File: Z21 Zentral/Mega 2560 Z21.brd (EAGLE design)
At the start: 122 x 122.3 mm, 144 parts, among them IC1 TLE5205-2G, IC2 74AC244DW, IC3 LM358D, IC5 FT232RL, IC6 LTC485S, J1 RJ11, J2 RJ11, J3 RJ11, J5 RJ45-6L-B, J6 USB_MINI-B_SMT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

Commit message: Add files via upload
Changed 6 way power connector to allow connector to fit
Added PFET on input instead of Diode
Tidied up PCB Legends
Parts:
- removed D1: P600, diode:P6-15
- added D5: (no value), diode:SOT23
- added Q9: FDD4141TO252, transistor-fet:TO252
- added R31: 100k, rcl:R0603
- X9: device con-wago-508:W237-6P -> con-wago-500:W237-136
- moved B1 2.75 mm to (34.0, 97.0)
- moved K1 2.25 mm to (46.5, 97.5)
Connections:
- new net N$22: D5.1, Q9.1, R31.1
- net +18V: now also D5.3, Q9.2; no longer D1.C
- net GND: now also R31.2
- net N$23: now also Q9.3; no longer D1.A
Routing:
- net +18V: track 154.7 -> 187.4 mm
- net +12V: track 146.6 -> 151.4 mm
- net N$22: track 0.00 -> 3.62 mm
- net N$23: track 7.96 -> 11.3 mm
- net VCCIO: track 158.1 -> 154.9 mm
- net N$32: track 22.6 -> 24.7 mm
- net N$34: track 30.1 -> 32.1 mm
- net N$39: track 11.3 -> 9.79 mm
- net SSHORT: track 72.0 -> 73.2 mm
- net N$25: track 68.1 -> 67.0 mm
- net S2: track 62.0 -> 62.9 mm
- net XPB: track 65.5 -> 65.0 mm
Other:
- board text added: "Arduino Z21 DCC Zentrale IoT Tech & Philipp Gahtow July 2019"
- board text added: "S88"
- board text removed: "Arduino Z21 DCC Zentrale IoT Tech & Philipp Gahtow October 2018"

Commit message: Add files via upload
Added P Channel FET, replacing Diode
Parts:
- added IC4: (no value), v-reg:78XXS
- moved LED6 21.2 mm to (20.0, 78.0), turned to 90 degrees
- moved R51 17.9 mm to (20.0, 82.0)
- moved C11 0.90 mm to (18.2, 94.0)
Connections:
- net +12V: now also IC4.OUT
- net +18V: now also IC4.IN
- net GND: now also IC4.GND
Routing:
- net +18V: track 187.4 -> 172.8 mm
- net +12V: track 151.4 -> 153.6 mm
- net N$34: track 32.1 -> 30.2 mm
- net XNET_S/R: track 53.0 -> 51.1 mm
- net LN_OUT: track 78.7 -> 77.2 mm
- net XNET_TX: track 33.3 -> 32.0 mm
- net N$32: track 24.7 -> 23.3 mm
- net LN_IN: track 74.9 -> 73.9 mm
- net LN_RECEIVE: track 58.2 -> 57.3 mm

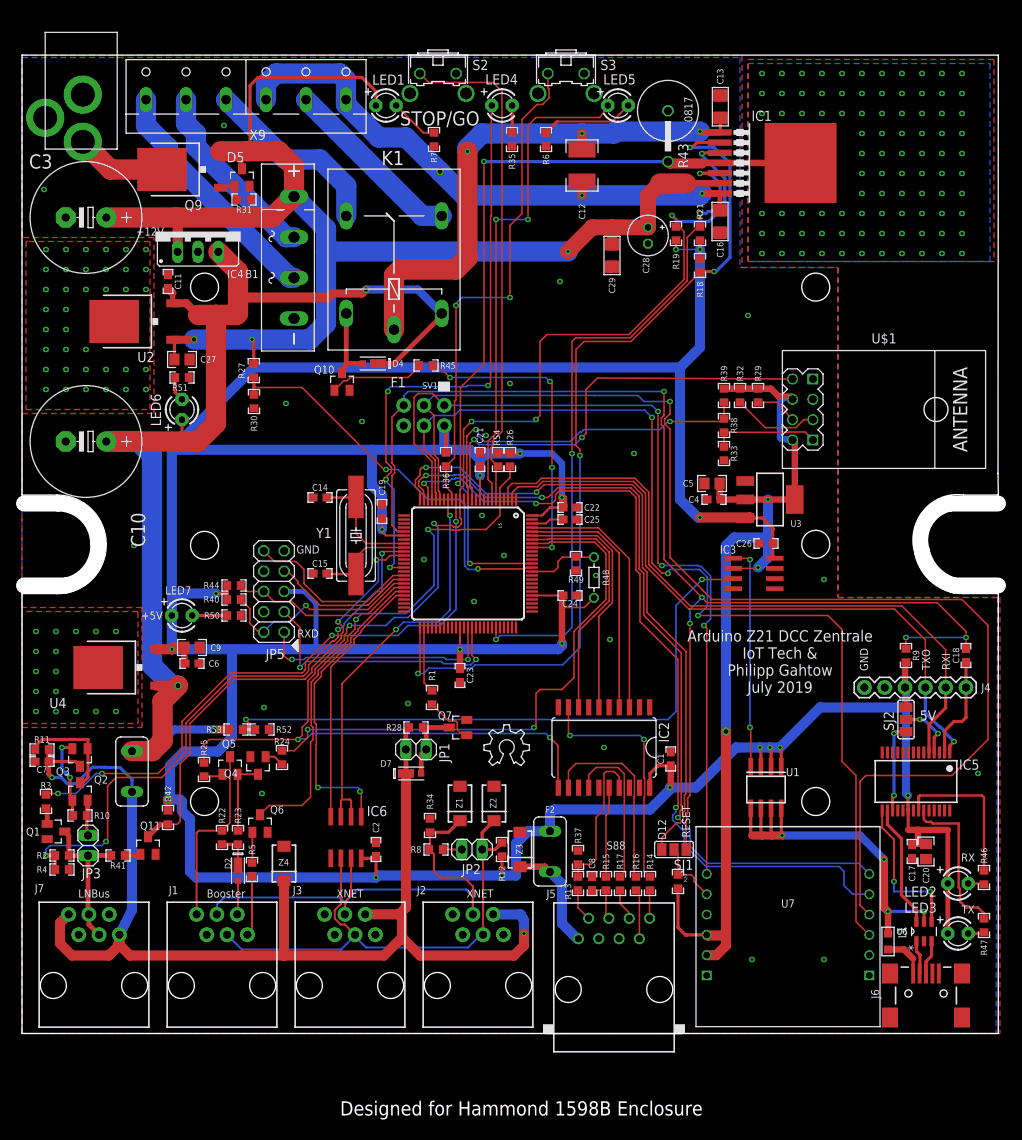
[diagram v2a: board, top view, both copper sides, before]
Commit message: Changed power connector and minor moves of components
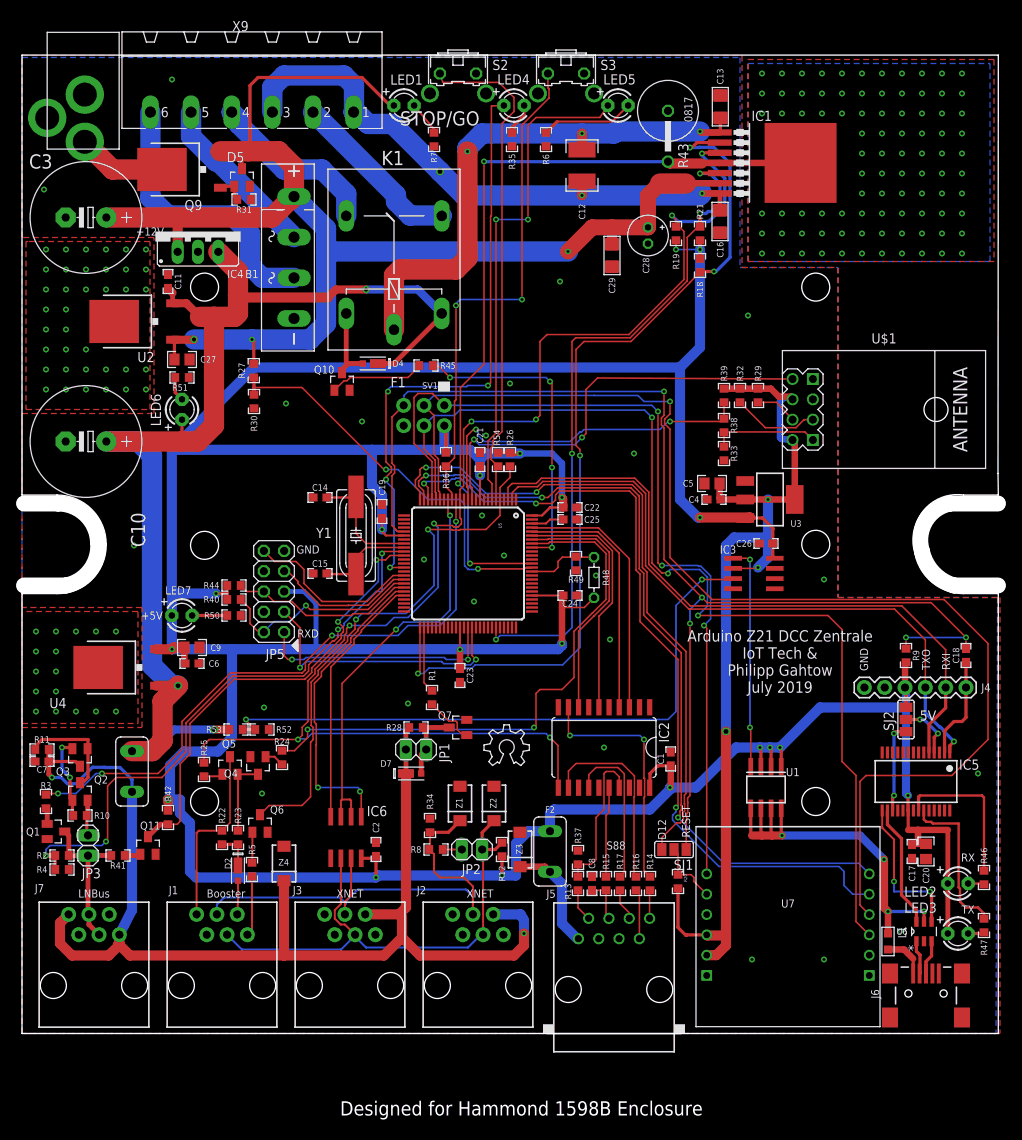
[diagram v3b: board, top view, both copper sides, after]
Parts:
- X9: value (none) -> MSTBA6; device con-wago-500:W237-136 -> con-phoenix-508:MSTBA6
- moved S2 2.50 mm to (54.5, 118.8)
- moved X9 2.37 mm to (28.8, 120.2), turned to 180 degrees
- moved LED1 2.25 mm to (47.8, 116.0)
- moved LED4 1.50 mm to (61.5, 116.0)
- moved U$2 0.25 mm to (7.75, 120.8)
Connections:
- net N$26: now also X9.1, X9.3; no longer X9.4, X9.6
- net N$32: now also K1.S; no longer B1.AC1
- net N$34: now also X9.6; no longer X9.1
- net N$37: now also X9.4; no longer X9.3
- net N$40: now also B1.AC1; no longer K1.S
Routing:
- net N$34: track 30.2 -> 35.2 mm
- net N$40: track 23.0 -> 21.1 mm
- net N$29: track 6.14 -> 4.30 mm
- net N$37: track 23.3 -> 21.7 mm
- net SSHORT: track 73.2 -> 74.7 mm
- net N$32: track 23.3 -> 21.9 mm
- net SCK: track 157.0 -> 155.7 mm
- net !INT: track 103.1 -> 101.9 mm
- net +18V: track 172.8 -> 174.0 mm
- net CS: track 104.8 -> 103.9 mm
- net S2: track 62.9 -> 63.5 mm
- net N$3: track 3.41 -> 4.02 mm
